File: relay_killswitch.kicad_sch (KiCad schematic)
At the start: 4 parts, among them Q3 BSN20, Q5 DMG2301L

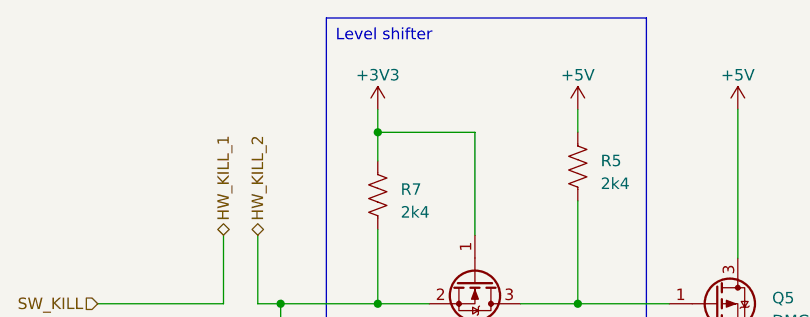
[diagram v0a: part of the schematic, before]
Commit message: convert from 2 -> 4 layer board, reduce vias and traces, currently no errors when running DRC
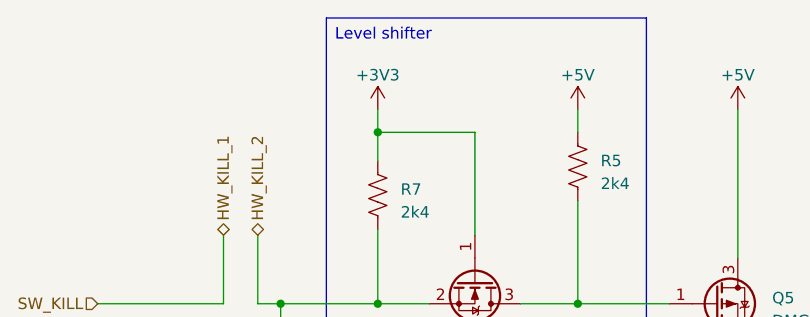
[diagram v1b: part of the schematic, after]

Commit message: Removed AND gate kill switch, added HW_KILL_3 and HW_KILL_4 in series in front of kill switch relay, changed net ground plane from BATT to GND (fix), removed kill switch footprint
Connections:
- net HW_KILL_2: no longer Q3.2 (S), R7.2
- new net HW_KILL_4: Q3.2 (S), R7.2
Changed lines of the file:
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@@
 	(wire
 		(pts
-			(xy 27.94 49.53) (xy 27.94 41.91)
+			(xy 19.05 49.53) (xy 19.05 41.91)
+		)
+		(stroke
+			(width 0)
+			(type default)
+		)
+	)
+	(wire
+		(pts
+			(xy 27.94 41.91) (xy 27.94 49.53)
+		)
+		(stroke
+			(width 0)
+			(type default)
+		)
+	)
+	(wire
+		(pts
+			(xy 22.86 49.53) (xy 27.94 49.53)
+		)
+		(stroke
+			(width 0)
+			(type default)
+		)
+	)
+	(wire
+		(pts
+			(xy 60.96 49.53) (xy 67.31 49.53)
 		)
 		(stroke
@@
 	(wire
 		(pts
-			(xy 60.96 49.53) (xy 67.31 49.53)
-		)
-		(stroke
-			(width 0)
-			(type default)
-		)
-	)
-	(wire
-		(pts
 			(xy 34.29 56.515) (xy 34.29 49.53)
 		)
@@
 	(wire
 		(pts
+			(xy 31.75 41.91) (xy 31.75 49.53)
+		)
+		(stroke
+			(width 0)
+			(type default)
+		)
+	)
+	(wire
+		(pts
 			(xy 67.31 49.53) (xy 77.47 49.53)
 		)
@@
 	(wire
 		(pts
-			(xy 31.75 41.91) (xy 31.75 49.53)
+			(xy 22.86 41.91) (xy 22.86 49.53)
 		)
 		(stroke
@@
 	(wire
 		(pts
-			(xy 13.97 49.53) (xy 27.94 49.53)
+			(xy 13.97 49.53) (xy 19.05 49.53)
 		)
 		(stroke
@@
 	)
 	(hierarchical_label "HW_KILL_2"
+		(shape bidirectional)
+		(at 22.86 41.91 90)
+		(effects
+			(font
+				(size 1.27 1.27)
+			)
+			(justify left)
+		)
+	)
+	(hierarchical_label "HW_KILL_4"
 		(shape bidirectional)
 		(at 31.75 41.91 90)
@@
 	(hierarchical_label "HW_KILL_1"
 		(shape bidirectional)
+		(at 19.05 41.91 90)
+		(effects
+			(font
+				(size 1.27 1.27)
+			)
+			(justify left)
+		)
+	)
+	(hierarchical_label "HW_KILL_3"
+		(shape bidirectional)
 		(at 27.94 41.91 90)
